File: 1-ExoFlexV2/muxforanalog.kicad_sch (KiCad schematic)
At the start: 8 parts

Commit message: Schématisation terminée
- Schéma terminé
- Passage vers le PCB
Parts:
- J130, J131: renamed from J?; value Jmp -> Jumper; footprint (none) -> Connector_PinSocket_2.54mm:PinSocket_1x03_P2.54mm_Vertical; DESCRIPTION (none) -> CONN HEADER VERT 3POS 2.54MM; MANUFACTURER (none) -> Würth Elektronik; PACKAGE (none) -> Square 0.100" (2.54mm); PART NUMBER (none) -> 61300311121; TYPE (none) -> Through Hole
- R208, R209: renamed from R?; value 1k -> 1k 1% 1/10W; footprint Resistor_SMD:R_0805_2012Metric -> Resistor_SMD:R_0402_1005Metric; DESCRIPTION (none) -> 1 kOhms ±1% 0.1W, 1/10W Chip Resistor 0402 (1005 Metric) Au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; MANUFACTURER (none) -> Panasonic Electronic Components; PACKAGE (none) -> 0402 (1005 Metric); PART NUMBER (none) -> ERJ-2RKF1001X; TYPE (none) -> SMD
- RV35, RV36: renamed from RV?; value 523Ω -> Trim 1k; DESCRIPTION (none) -> Trimmer 1k 0,5W PC PIN TOP; MANUFACTURER (none) -> Bourns Inc.; PACKAGE (none) -> Rectangular - 0.275" x 0.260" Face; PART NUMBER (none) -> 3362P-1-102LF; TYPE (none) -> Through Hole
- U121, U122: renamed from U?; value 74HC4051PW -> MUX 8:1; DESCRIPTION (none) -> 1 Circuit IC Switch 8:1 120Ohm 16-TSSOP; MANUFACTURER (none) -> Nexperia USA Inc.; PACKAGE (none) -> 16-TSSOP (0.173", 4.40mm Width); PART NUMBER (none) -> 74HC4051PW,118; TYPE (none) -> SMD
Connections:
- net GND: now also U121.8 (GND)
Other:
- note added: "2xMUX8_1 : 5V @ 100mA 2xPot1k : 5V @ 20mA Total current : 5V @ 125mA"
- note added: "523Ω"
- note removed: "2xMUX8_1 : 5V @ 100mA Total current : 5V @ 100mA"

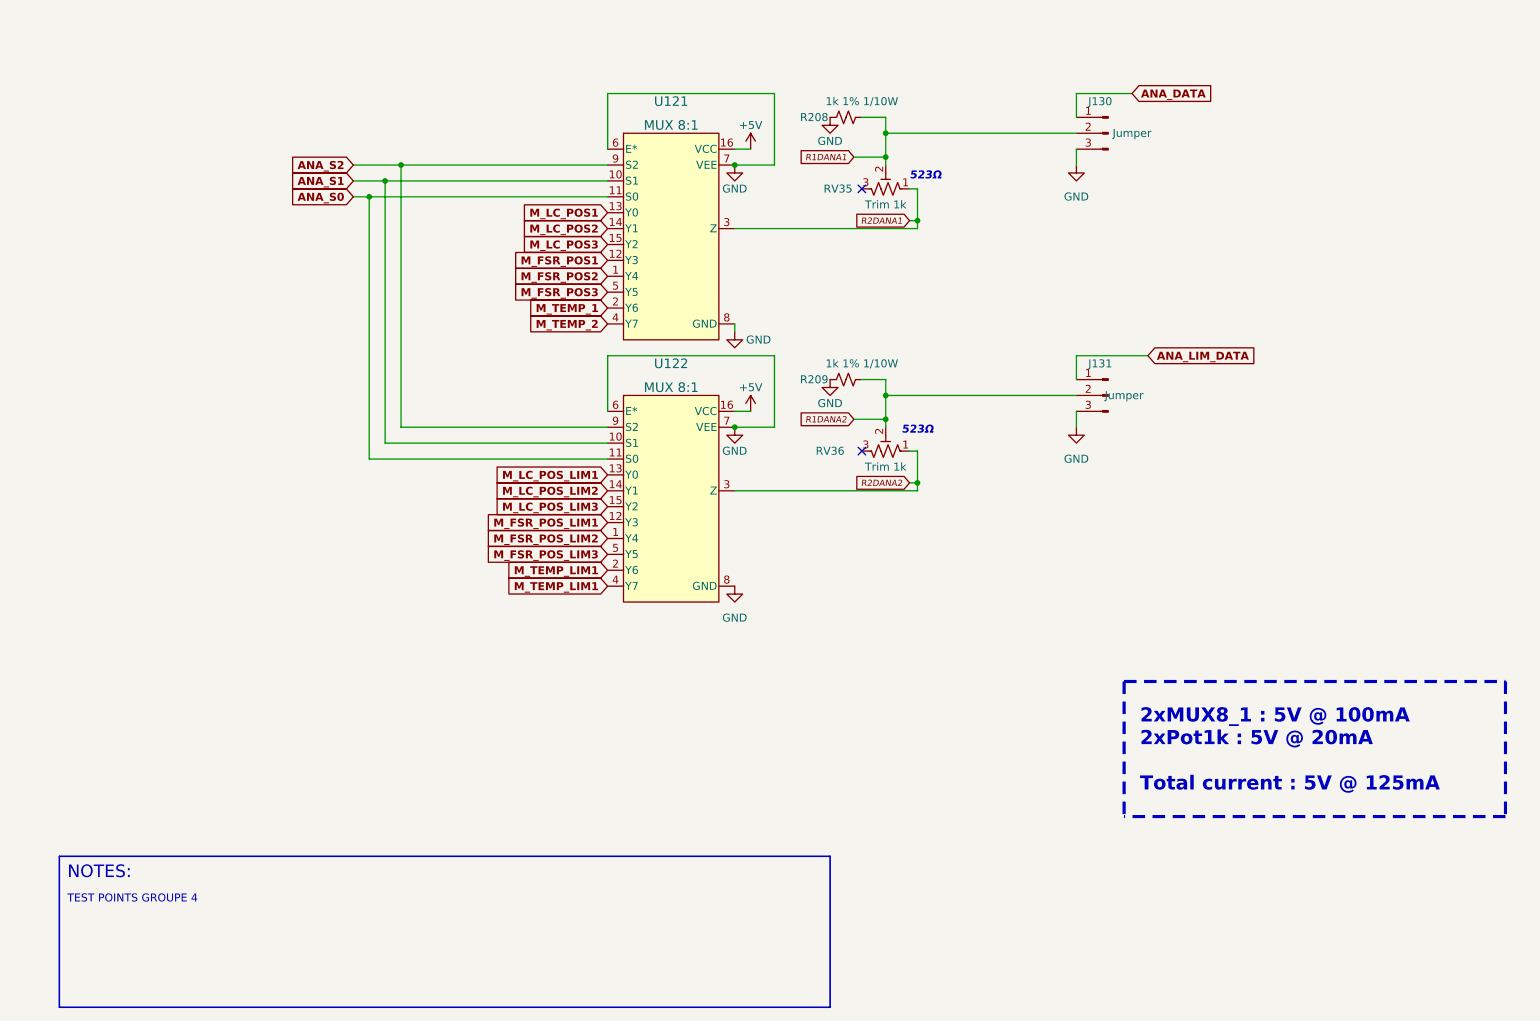
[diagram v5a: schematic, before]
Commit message: Finalisation 3
- Changement des régulateur de tension
- Retrait de test point inutile
- Changement de jumper mal positionner
- Ajout de Mounting holes et fiducial
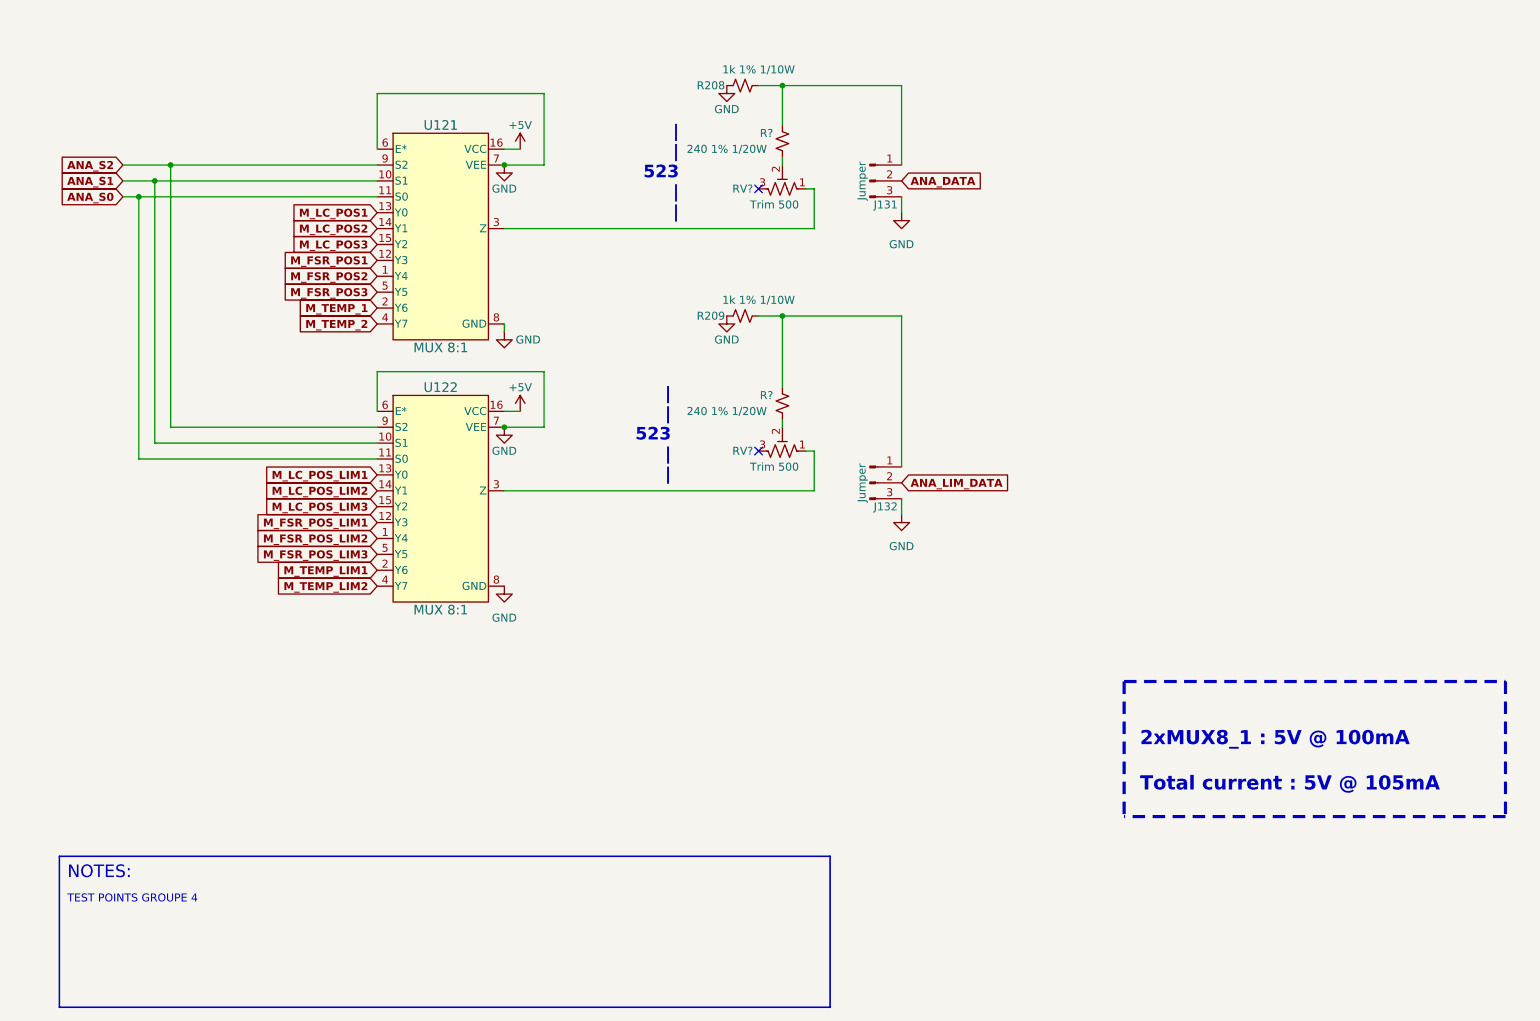
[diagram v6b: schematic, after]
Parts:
- removed RV35, RV36: Trim 1k, FootPrint:TRIM_3362P-1-102LF, symbol Device:R_Potentiometer_Trim_US
- added R? (x2): 240 1% 1/20W, Resistor_SMD:R_0201_0603Metric, symbol Device:R_Small_US
- added RV? (x2): Trim 500, FootPrint:TRIM_3296W-1-501LF, symbol Device:R_Potentiometer_Trim_US
- J131: renamed from J130; footprint Connector_PinSocket_2.54mm:PinSocket_1x03_P2.54mm_Vertical -> Connector_PinHeader_2.54mm:PinHeader_1x03_P2.54mm_Vertical
- J132: renamed from J131; footprint Connector_PinSocket_2.54mm:PinSocket_1x03_P2.54mm_Vertical -> Connector_PinHeader_2.54mm:PinHeader_1x03_P2.54mm_Vertical
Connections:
- net ANA_DATA: now also J131.2 (Pin_2); no longer J131.1 (Pin_1)
- net ANA_LIM_DATA: now also J132.2 (Pin_2); no longer J132.1 (Pin_1)
- net M_TEMP_LIM1: no longer U122.4 (Y7)
- net R1DANA1: no longer names the net of R208.2
- net R1DANA1: now also J131.1 (Pin_1), R?.2; no longer J131.2 (Pin_2)
- net R1DANA2: no longer names the net of R209.2
- net R1DANA2: now also J132.1 (Pin_1), R?.2; no longer J132.2 (Pin_2)
- net R2DANA1: no longer names the net of U121.3 (Z)
- net R2DANA1: now also RV?.1
- net R2DANA2: no longer names the net of U122.3 (Z)
- net R2DANA2: now also RV?.1
- new net: R?.1, RV?.2 (x2)
- new net M_TEMP_LIM2: U122.4 (Y7)
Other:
- note added: "2xMUX8_1 : 5V @ 100mA Total current : 5V @ 105mA"
- note added: "| | 523 | |"
- note removed: "2xMUX8_1 : 5V @ 100mA 2xPot1k : 5V @ 20mA Total current : 5V @ 125mA"
- note removed: "523Ω"
- moved on the sheet: J131, J132, R208, R209, U121, U122

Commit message: Finalisation schéma FIN
- Changement des uméro pour les inverseurs
- Changement des connecteur et début de placement
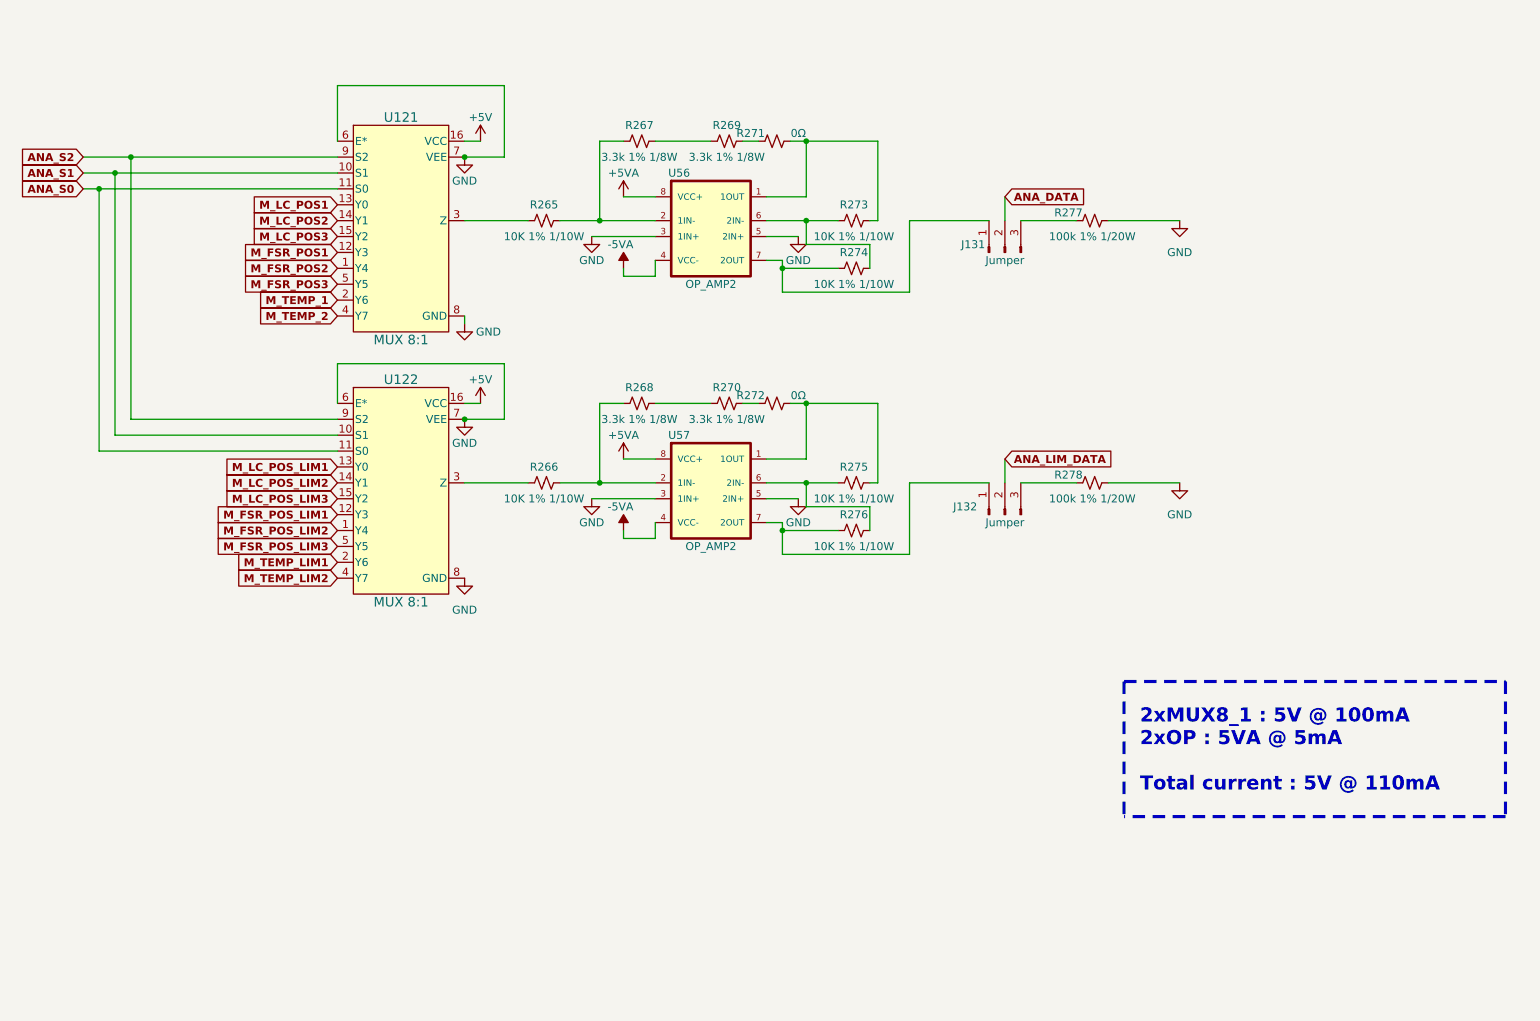
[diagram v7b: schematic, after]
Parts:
- removed R208, R209: 1k 1% 1/10W, Resistor_SMD:R_0402_1005Metric, symbol Device:R_Small_US
- removed R? (x2): 240 1% 1/20W, Resistor_SMD:R_0201_0603Metric, symbol Device:R_Small_US
- removed RV? (x2): Trim 500, FootPrint:TRIM_3296W-1-501LF, symbol Device:R_Potentiometer_Trim_US
- added R265, R266, R273, R274, R275, R276: 10K 1% 1/10W, Resistor_SMD:R_0603_1608Metric, symbol Device:R_Small_US
- added R267, R268, R269, R270: 3.3k 1% 1/8W, Resistor_SMD:R_0805_2012Metric, symbol Device:R_Small_US
- added R271, R272: 0Ω, Resistor_SMD:R_0805_2012Metric, symbol Device:R_Small_US
- added R277, R278: 100k 1% 1/20W, Resistor_SMD:R_0201_0603Metric, symbol Device:R_Small_US
- added U56, U57: OP_AMP2, FootPrintLib:SOIC127P599X175-8N, symbol SymLib:TL072IDR
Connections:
- net GND: now also R277.2, R278.2, U56.3 (1IN+), U56.5 (2IN+), U57.3 (1IN+), U57.5 (2IN+); no longer J131.3 (Pin_3), J132.3 (Pin_3)
- net at J132.1 (Pin_1): now also R276.1, U57.7 (2OUT)
- net at J131.1 (Pin_1): now also R274.1, U56.7 (2OUT)
- net at U122.3 (Z): now also R266.1
- net at U121.3 (Z): now also R265.1
- new net: J131.3 (Pin_3), R277.1
- new net: R272.2, R275.2, U57.1 (1OUT)
- new net: R266.2, R268.1, U57.2 (1IN-)
- new net: R275.1, R276.2, U57.6 (2IN-)
- new net: R273.1, R274.2, U56.6 (2IN-)
- new net: R265.2, R267.1, U56.2 (1IN-)
- new net: R267.2, R269.1
- new net: R271.2, R273.2, U56.1 (1OUT)
- new net: R268.2, R270.1
- new net: R270.2, R272.1
- new net: R269.2, R271.1
- new net: J132.3 (Pin_3), R278.1
- new net +5VA: U56.8 (VCC+), U57.8 (VCC+)
- new net -5VA: U56.4 (VCC-), U57.4 (VCC-)
- no-connect marks 2 -> 0
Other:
- note added: "2xMUX8_1 : 5V @ 100mA 2xOP : 5VA @ 5mA Total current : 5V @ 110mA"
- note removed: "2xMUX8_1 : 5V @ 100mA Total current : 5V @ 105mA"
- note removed: "NOTES:"
- note removed: "TEST POINTS GROUPE 4"
- note removed: "| | 523 | |"
- moved on the sheet: J131, J132, U121, U122

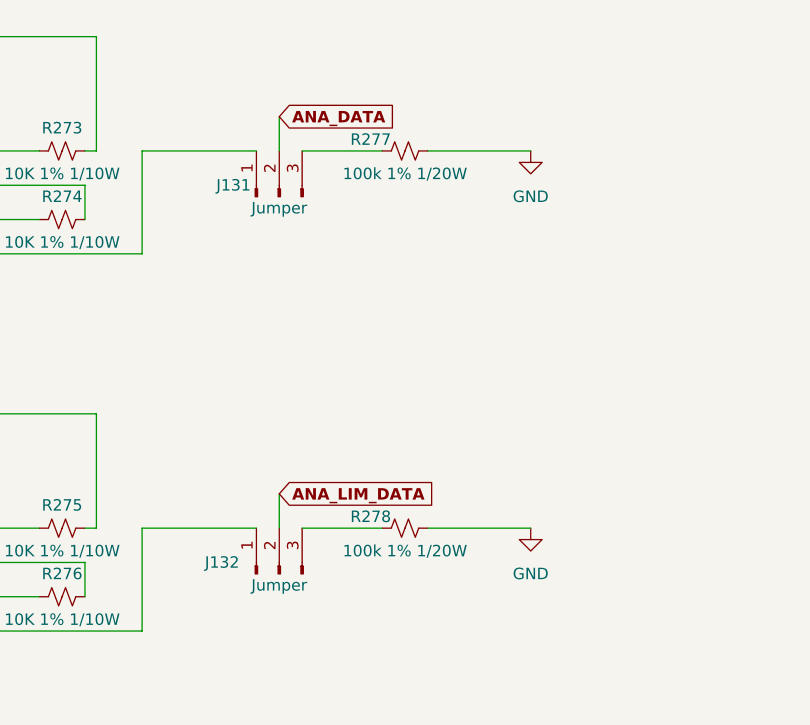
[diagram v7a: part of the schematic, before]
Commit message: Modification Schéma + Layout
- Ajout de RC potentiel entre les capteur de torque et l'ampli d'instru
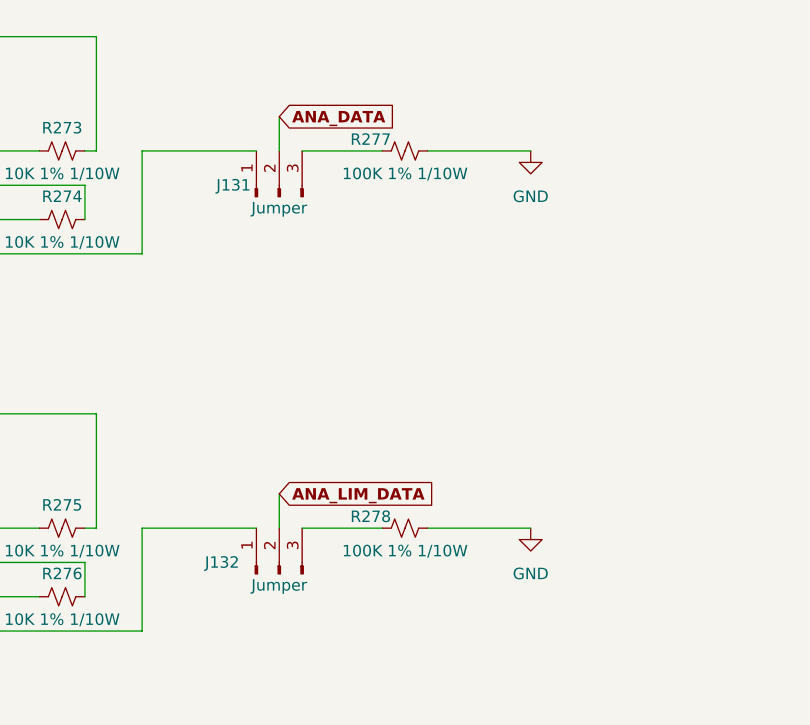
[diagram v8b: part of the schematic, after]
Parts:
- R277, R278: value 100k 1% 1/20W -> 100K 1% 1/10W; footprint Resistor_SMD:R_0201_0603Metric -> Resistor_SMD:R_0603_1608Metric; DESCRIPTION 100 kOhms ±1% 0.05W, 1/20W Chip Resistor 0201 (0603 Metric)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 -> 100 kOhms ±1% 0.1W, 1/10W Chip Resistor 0603 (1608 Metric) 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
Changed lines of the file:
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@@
     (in_bom yes) (on_board yes)
     (property "Reference" "R277" (id 0) (at 209.55 67.31 90))
-    (property "Value" "100k 1% 1/20W" (id 1) (at 213.36 71.12 90))
-    (property "Footprint" "Resistor_SMD:R_0201_0603Metric" (id 2) (at 213.36 68.58 0)
+    (property "Value" "100K 1% 1/10W" (id 1) (at 213.36 71.12 90))
+    (property "Footprint" "Resistor_SMD:R_0603_1608Metric" (id 2) (at 213.36 68.58 0)
       (effects (font (size 1.27 1.27)) hide)
     )
@@
       (effects (font (size 1.27 1.27)) hide)
     )
-    (property "DESCRIPTION" "100 kOhms ±1% 0.05W, 1/20W Chip Resistor 0201 (0603 Metric) Thick Film" (id 8) (at 213.36 68.58 0)
+    (property "DESCRIPTION" "100 kOhms ±1% 0.1W, 1/10W Chip Resistor 0603 (1608 Metric) Automotive AEC-Q200 Thick Film" (id 8) (at 213.36 68.58 0)
       (effects (font (size 1.27 1.27)) hide)
     )
@@
     (in_bom yes) (on_board yes)
     (property "Reference" "R278" (id 0) (at 209.55 109.22 90))
-    (property "Value" "100k 1% 1/20W" (id 1) (at 213.36 113.03 90))
-    (property "Footprint" "Resistor_SMD:R_0201_0603Metric" (id 2) (at 213.36 110.49 0)
+    (property "Value" "100K 1% 1/10W" (id 1) (at 213.36 113.03 90))
+    (property "Footprint" "Resistor_SMD:R_0603_1608Metric" (id 2) (at 213.36 110.49 0)
       (effects (font (size 1.27 1.27)) hide)
     )
@@
       (effects (font (size 1.27 1.27)) hide)
     )
-    (property "DESCRIPTION" "100 kOhms ±1% 0.05W, 1/20W Chip Resistor 0201 (0603 Metric) Thick Film" (id 8) (at 213.36 110.49 0)
-      (effects (font (size 1.27 1.27)) hide)
-    )
+    (property "DESCRIPTION" "100 kOhms ±1% 0.1W, 1/10W Chip Resistor 0603 (1608 Metric) Automotive AEC-Q200 Thick Film" (id 8) (at 213.36 110.49 0)
+      (effects (font (size 1.27 1.27)) hide)
+    )
